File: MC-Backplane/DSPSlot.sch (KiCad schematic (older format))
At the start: 1 part, among them U12 374472

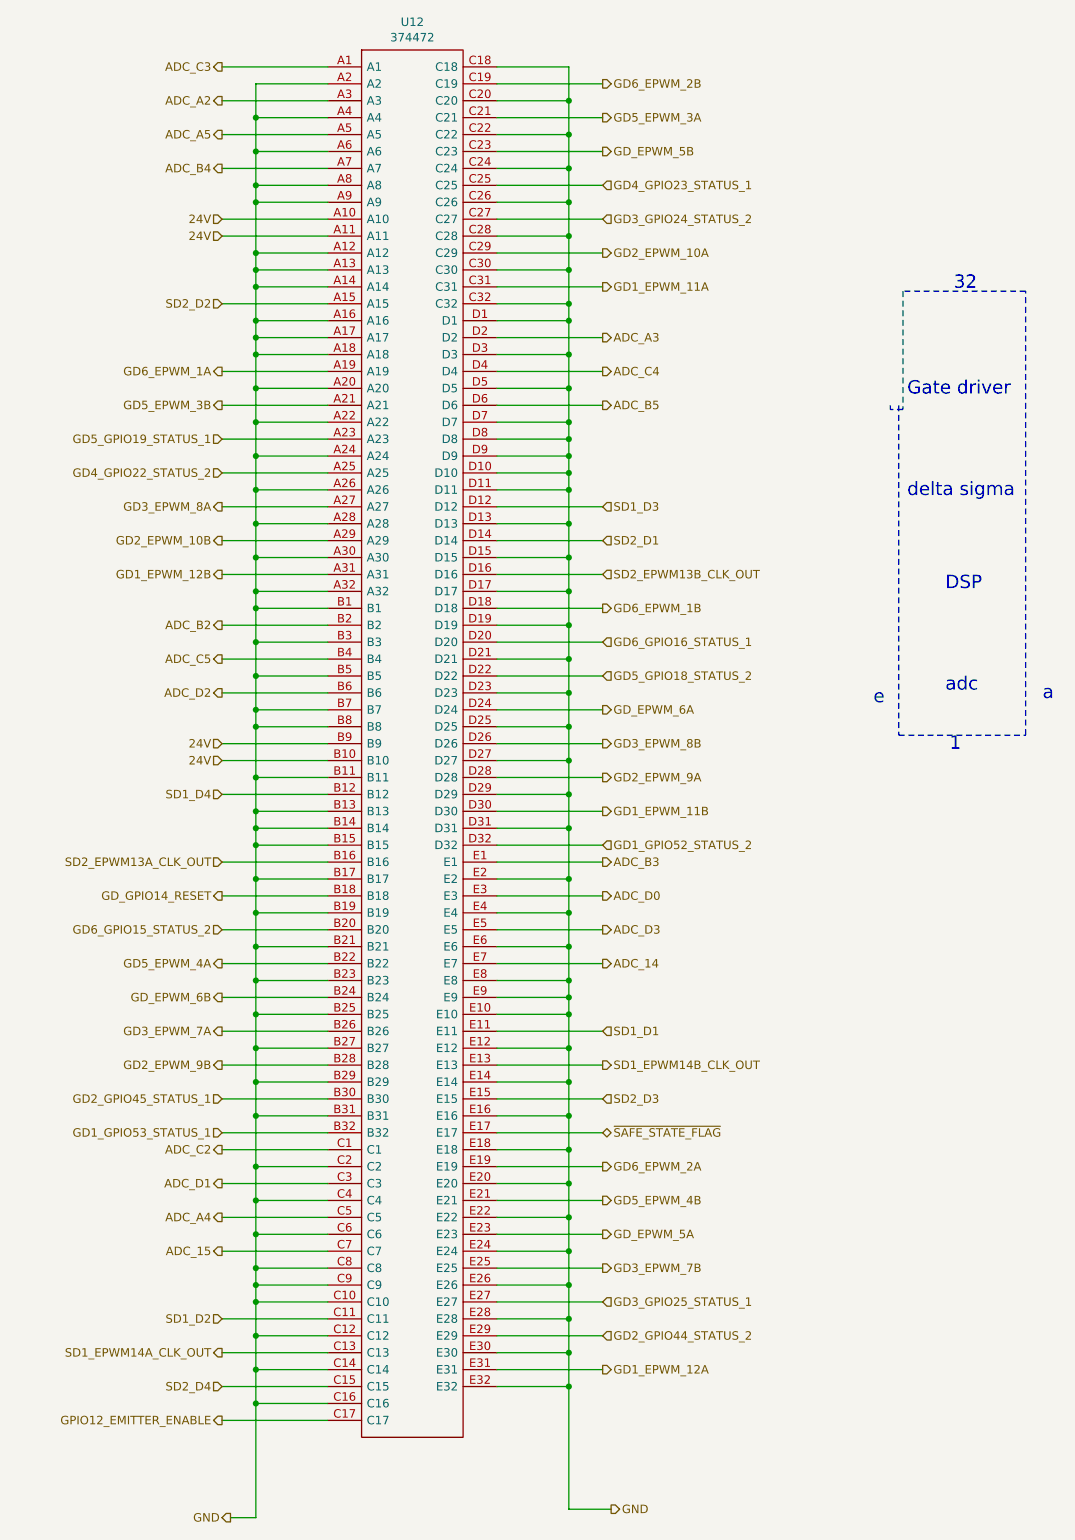
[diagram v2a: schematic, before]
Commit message: layout done: cleaning up and checking MH
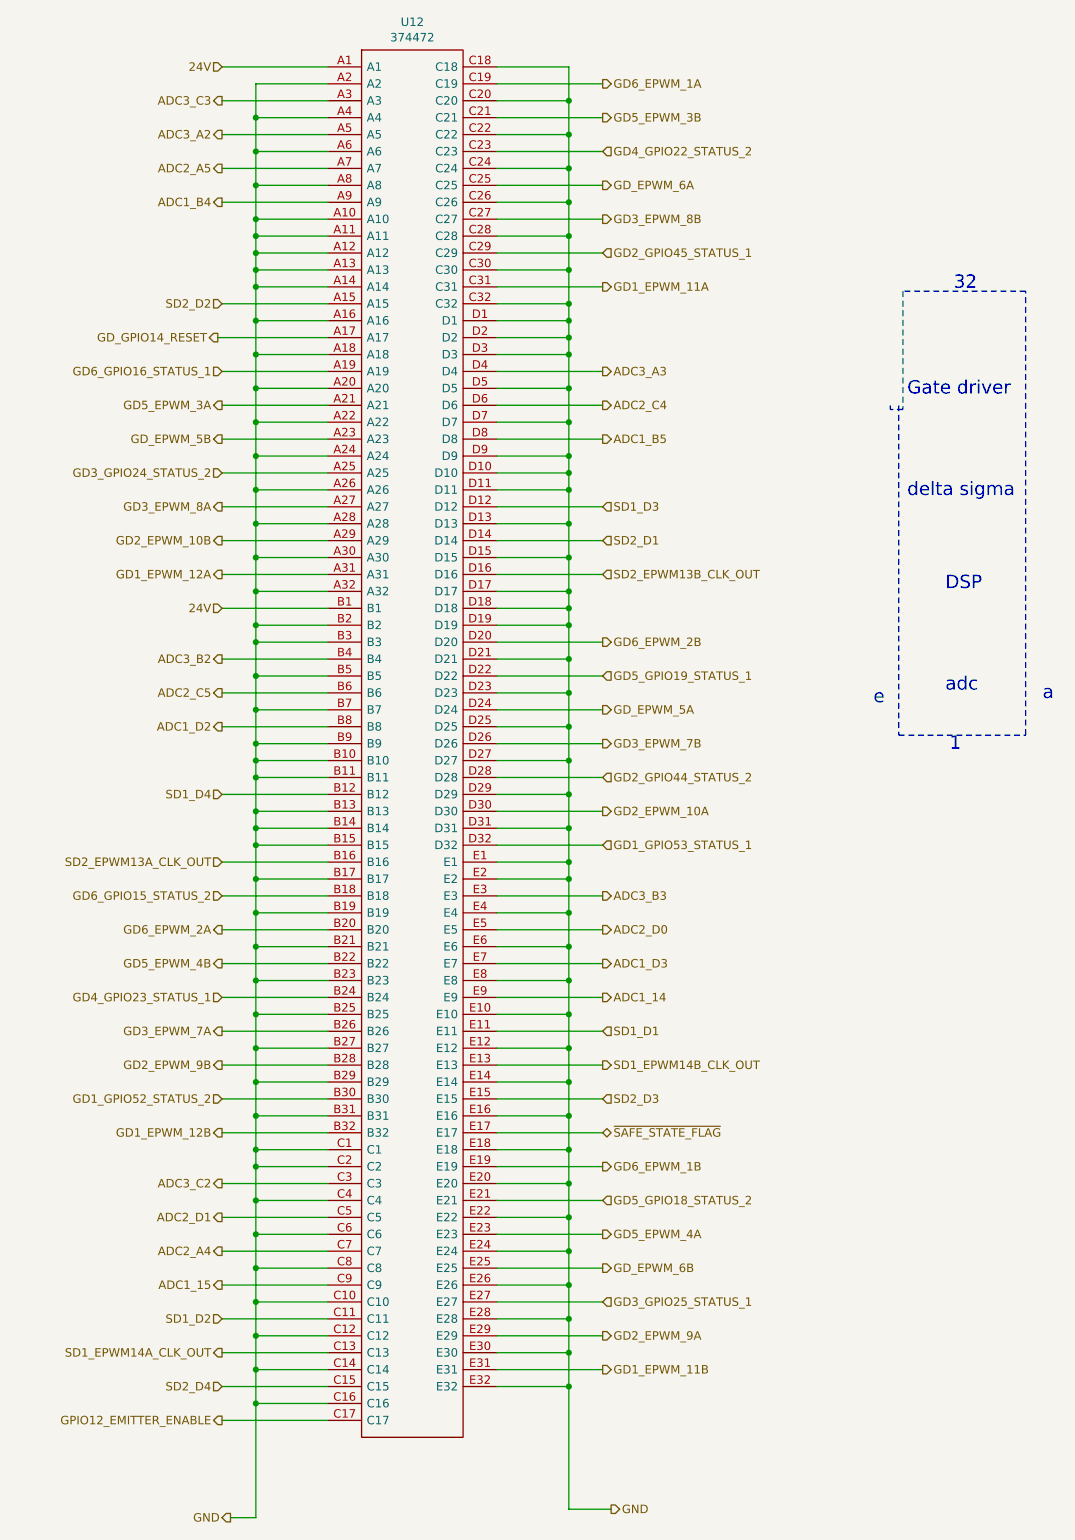
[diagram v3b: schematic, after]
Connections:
- net ADC_A3 is gone; now on net GND: U12.D2
- net ADC_B2 is gone; now on net GND: U12.B2
- net ADC_B3 is gone; now on net GND: U12.E1
- net ADC_C2 is gone; now on net GND: U12.C1
- net ADC_C3 is gone; now on net 24V: U12.A1
- net 24V: now also U12.B1; no longer U12.A10, U12.A11, U12.B10, U12.B9
- net GD1_EPWM_11B: now also U12.E31; no longer U12.D30
- net GD1_EPWM_12A: now also U12.A31; no longer U12.E31
- net GD1_EPWM_12B: now also U12.B32; no longer U12.A31
- net GD1_GPIO52_STATUS_2: now also U12.B30; no longer U12.D32
- net GD1_GPIO53_STATUS_1: now also U12.D32; no longer U12.B32
- net GD2_EPWM_10A: now also U12.D30; no longer U12.C29
- net GD2_EPWM_9A: now also U12.E29; no longer U12.D28
- net GD2_GPIO44_STATUS_2: now also U12.D28; no longer U12.E29
- net GD2_GPIO45_STATUS_1: now also U12.C29; no longer U12.B30
- net GD3_EPWM_7B: now also U12.D26; no longer U12.E25
- net GD3_EPWM_8B: now also U12.C27; no longer U12.D26
- net GD3_GPIO24_STATUS_2: now also U12.A25; no longer U12.C27
- net GD4_GPIO22_STATUS_2: now also U12.C23; no longer U12.A25
- net GD4_GPIO23_STATUS_1: now also U12.B24; no longer U12.C25
- net GD5_EPWM_3A: now also U12.A21; no longer U12.C21
- net GD5_EPWM_3B: now also U12.C21; no longer U12.A21
- net GD5_EPWM_4A: now also U12.E23; no longer U12.B22
- net GD5_EPWM_4B: now also U12.B22; no longer U12.E21
- net GD5_GPIO18_STATUS_2: now also U12.E21; no longer U12.D22
- net GD5_GPIO19_STATUS_1: now also U12.D22; no longer U12.A23
- net GD6_EPWM_1A: now also U12.C19; no longer U12.A19
- net GD6_EPWM_1B: now also U12.E19; no longer U12.D18
- net GD6_EPWM_2A: now also U12.B20; no longer U12.E19
- net GD6_EPWM_2B: now also U12.D20; no longer U12.C19
- net GD6_GPIO15_STATUS_2: now also U12.B18; no longer U12.B20
- net GD6_GPIO16_STATUS_1: now also U12.A19; no longer U12.D20
- net GD_EPWM_5A: now also U12.D24; no longer U12.E23
- net GD_EPWM_5B: now also U12.A23; no longer U12.C23
- net GD_EPWM_6A: now also U12.C25; no longer U12.D24
- net GD_EPWM_6B: now also U12.E25; no longer U12.B24
- net GD_GPIO14_RESET: now also U12.A17; no longer U12.B18
- net GND: now also U12.A10, U12.A11, U12.B10, U12.B9, U12.D18; no longer U12.A17, U12.A9, U12.B1, U12.B8, U12.C9, U12.D8, U12.E9
- net ADC_14 renamed ADC1_D3
- net ADC_15 renamed ADC2_A4
- net ADC_A2 renamed ADC3_C3
- net ADC_A4 renamed ADC2_D1
- net ADC_A5 renamed ADC3_A2
- net ADC_B4 renamed ADC2_A5
- net ADC_B5 renamed ADC2_C4
- net ADC_C4 renamed ADC3_A3
- net ADC_C5 renamed ADC3_B2
- net ADC_D0 renamed ADC3_B3
- net ADC_D1 renamed ADC3_C2
- net ADC_D2 renamed ADC2_C5
- net ADC_D3 renamed ADC2_D0
- new net ADC1_14: U12.E9
- new net ADC1_15: U12.C9
- new net ADC1_B4: U12.A9
- new net ADC1_B5: U12.D8
- new net ADC1_D2: U12.B8

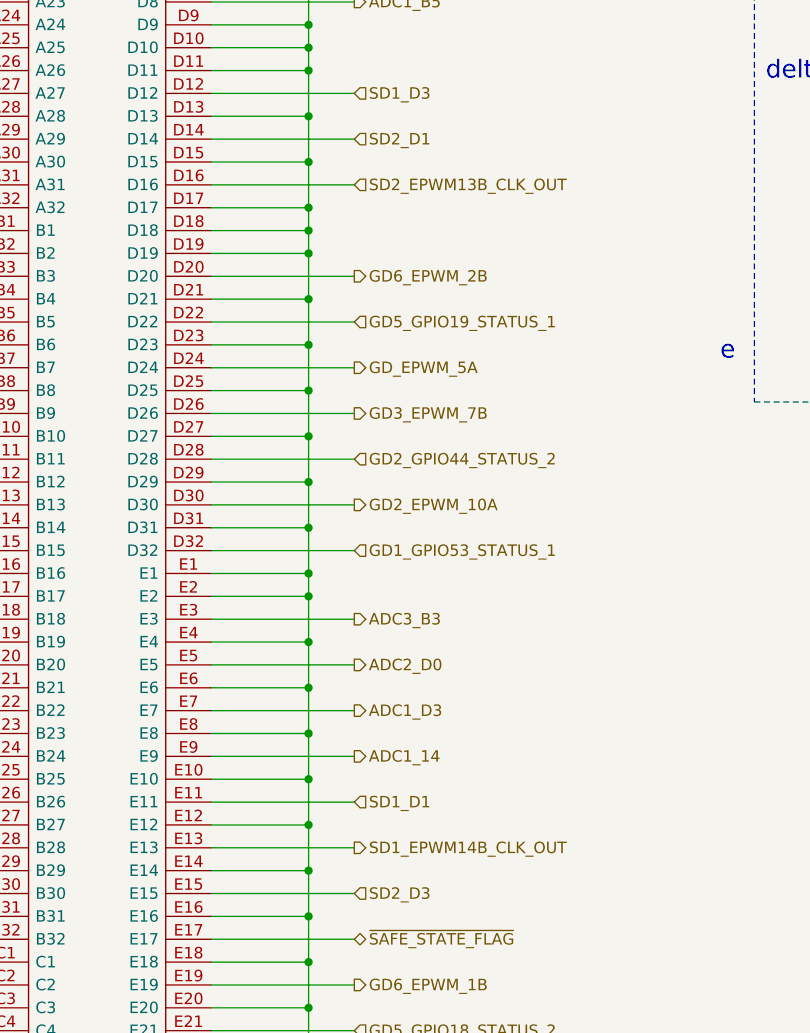
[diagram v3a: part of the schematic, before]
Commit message: spread tracks across available space
could still add some test points
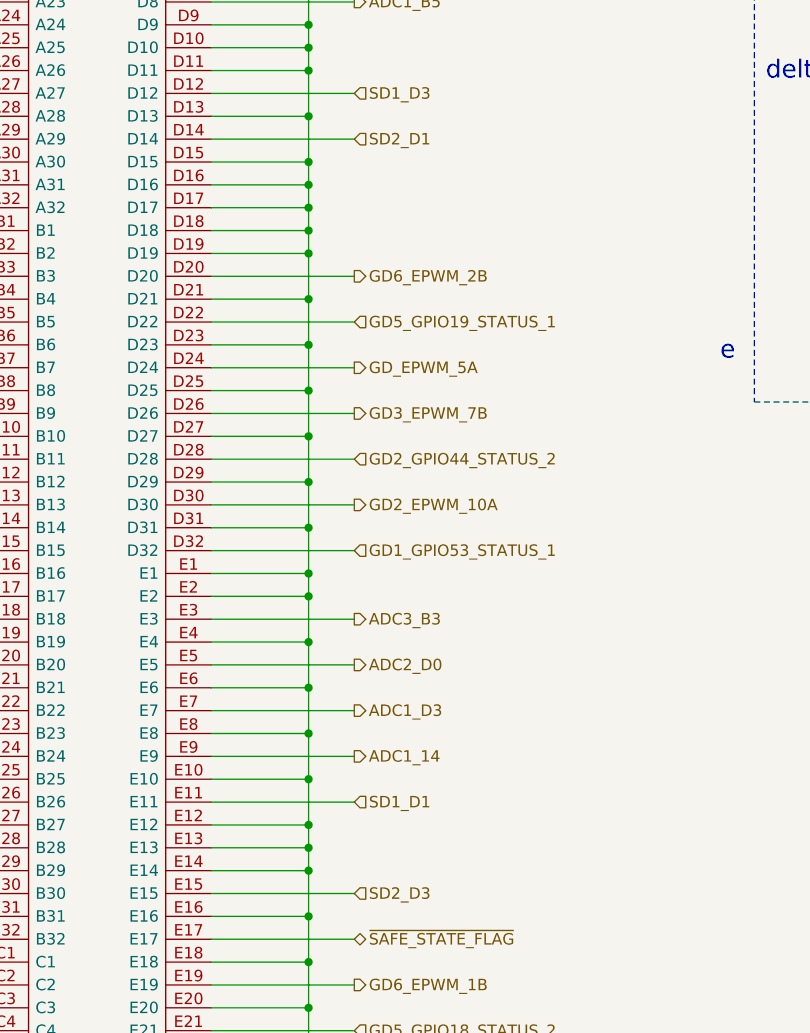
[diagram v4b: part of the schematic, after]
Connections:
- net SD1_EPWM14B_CLK_OUT is gone; now on net GND: U12.E13
- net SD2_EPWM13B_CLK_OUT is gone; now on net GND: U12.D16
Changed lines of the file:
@@
 Connection ~ 4800 4600
 Wire Wire Line
-	4800 4400 4800 4200
+	4800 4400 4800 4300
 Connection ~ 4800 4400
 Wire Wire Line
@@
 Connection ~ 4800 7300
 Wire Wire Line
-	4800 7100 4800 7300
+	4800 7100 4800 7200
 Connection ~ 4800 7100
 Wire Wire Line
@@
 	4375 7400 5000 7400
 Wire Wire Line
-	4375 7200 5000 7200
+	4375 7200 4800 7200
 Wire Wire Line
 	4375 6600 5000 6600
@@
 	4375 4500 4800 4500
 Wire Wire Line
-	4375 4300 5000 4300
+	4375 4300 4800 4300
 Wire Wire Line
 	4375 4100 5000 4100
@@
 Text HLabel 5000 5100 2    50   Output ~ 0
 GD_EPWM_5A
-Text HLabel 5000 7200 2    50   Output ~ 0
-SD1_EPWM14B_CLK_OUT
 Text HLabel 2750 8900 0    50   Output ~ 0
 SD1_EPWM14A_CLK_OUT
@@
 Text HLabel 5000 2600 2    50   Output ~ 0
 GD1_EPWM_11A
-Text HLabel 5000 4300 2    50   Input ~ 0
-SD2_EPWM13B_CLK_OUT
 Text HLabel 2750 6000 0    50   Input ~ 0
 SD2_EPWM13A_CLK_OUT
@@
 Wire Wire Line
 	2950 2200 2950 2300
+Connection ~ 4800 7200
+Wire Wire Line
+	4800 7200 4800 7300
+Connection ~ 4800 4300
+Wire Wire Line
+	4800 4300 4800 4200
 $EndSCHEMATC

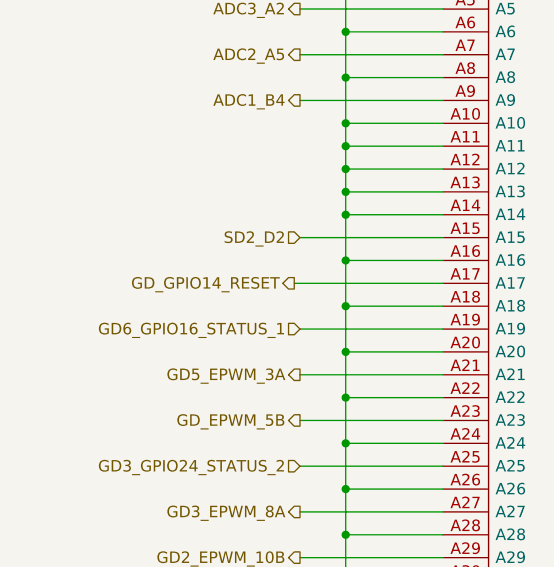
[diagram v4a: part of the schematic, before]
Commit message: added testpoints
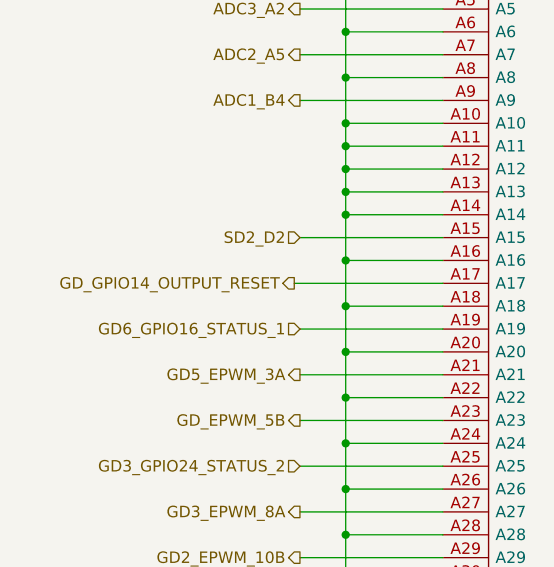
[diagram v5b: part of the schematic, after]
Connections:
- net GD_GPIO14_RESET renamed GD_GPIO14_OUTPUT_RESET
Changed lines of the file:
@@
 $EndComp
 Text HLabel 2725 2900 0    50   Output ~ 0
-GD_GPIO14_RESET
+GD_GPIO14_OUTPUT_RESET
 Text HLabel 5000 1400 2    50   Output ~ 0
 GD6_EPWM_1A
